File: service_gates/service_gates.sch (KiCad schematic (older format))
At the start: 1 part, among them P1 DIN_41612_128P

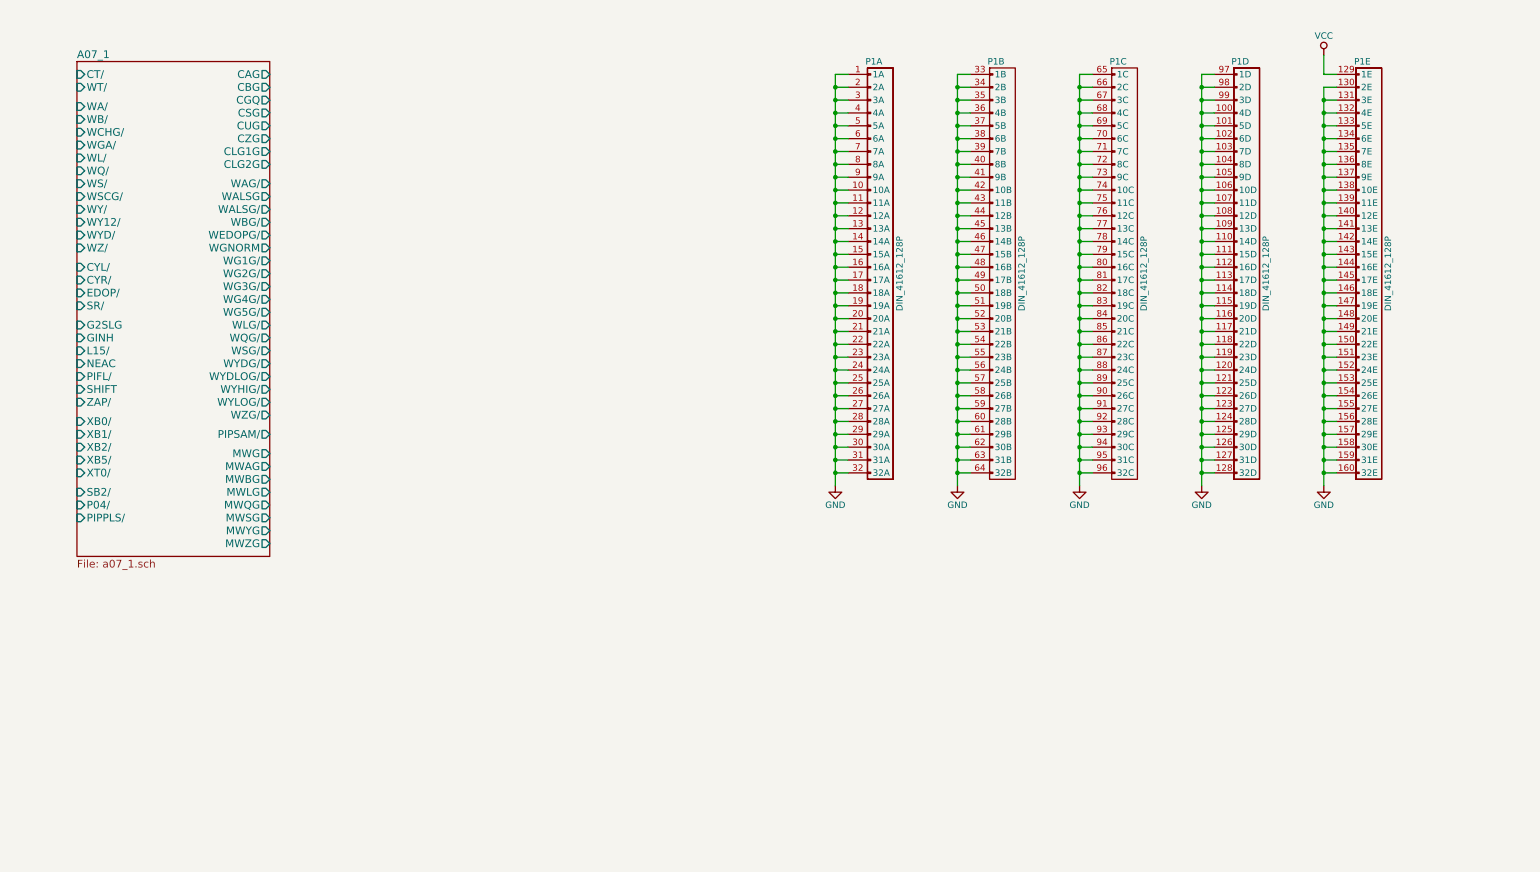
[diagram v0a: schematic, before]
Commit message: Page 2 of the service gates, including some service logic taken from modules 14 and 24 (page 1 got some updates too)
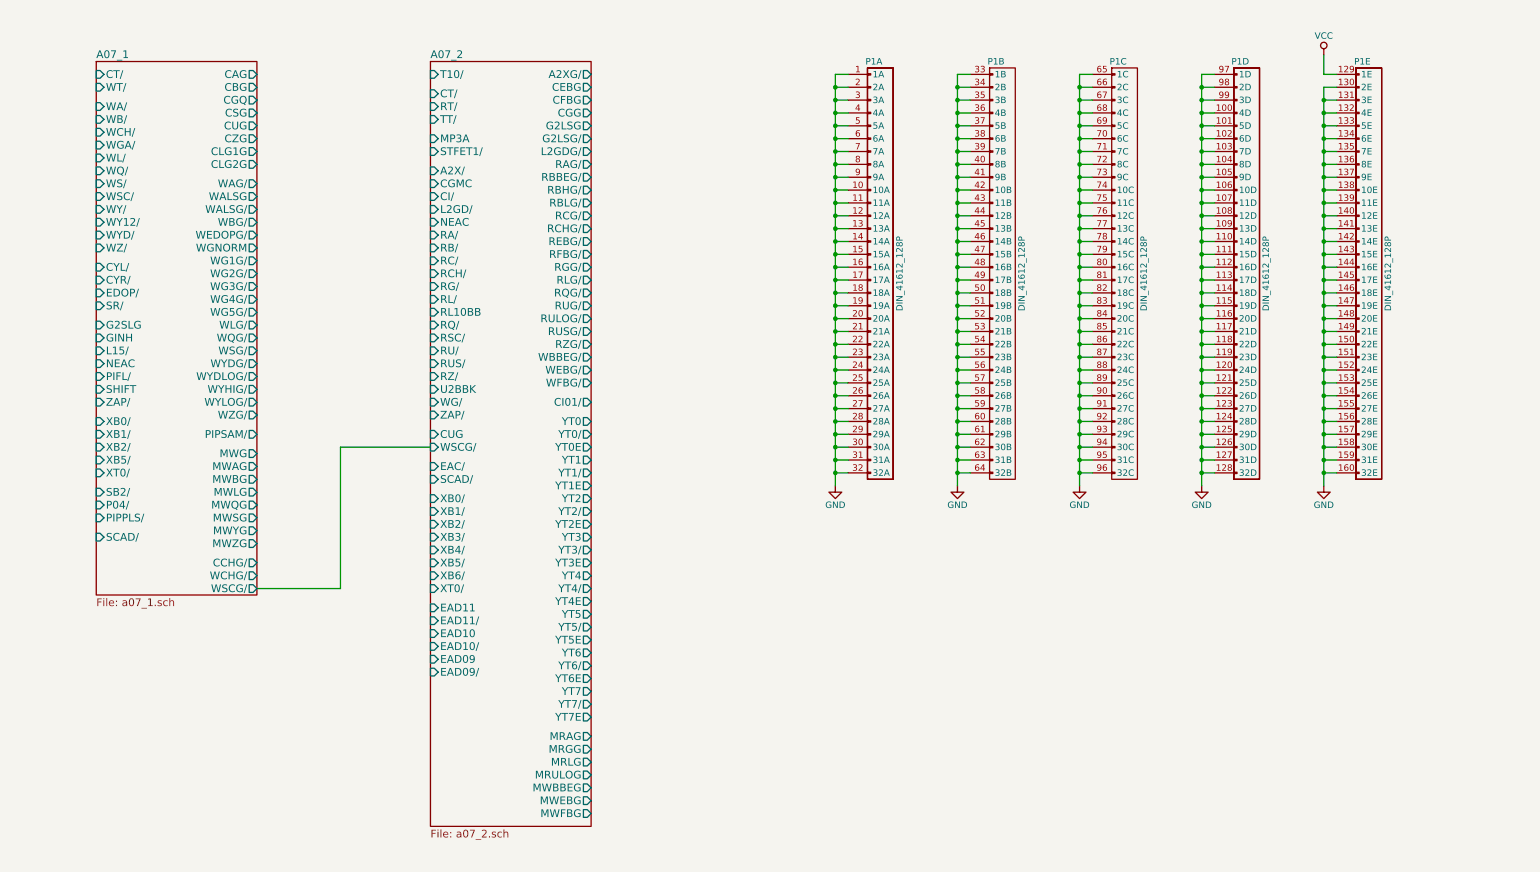
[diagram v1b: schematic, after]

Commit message: Tied in module 7, and corrected lots of errors.
Off the top of my head:
* T12DC/ not actually connected to restart logic in A02-2
* IC12/ and IC13 schematic errors
* Lots of gates moved from later modules up to modules 2-7
* YT0..7 logic dropped from 7, it belongs in 14
* Lots of missing signal breakouts
* ...probably some other things, I should keep a list as I go

All control pulses associated with GOJ1 now behave correctly during
GOJ1.
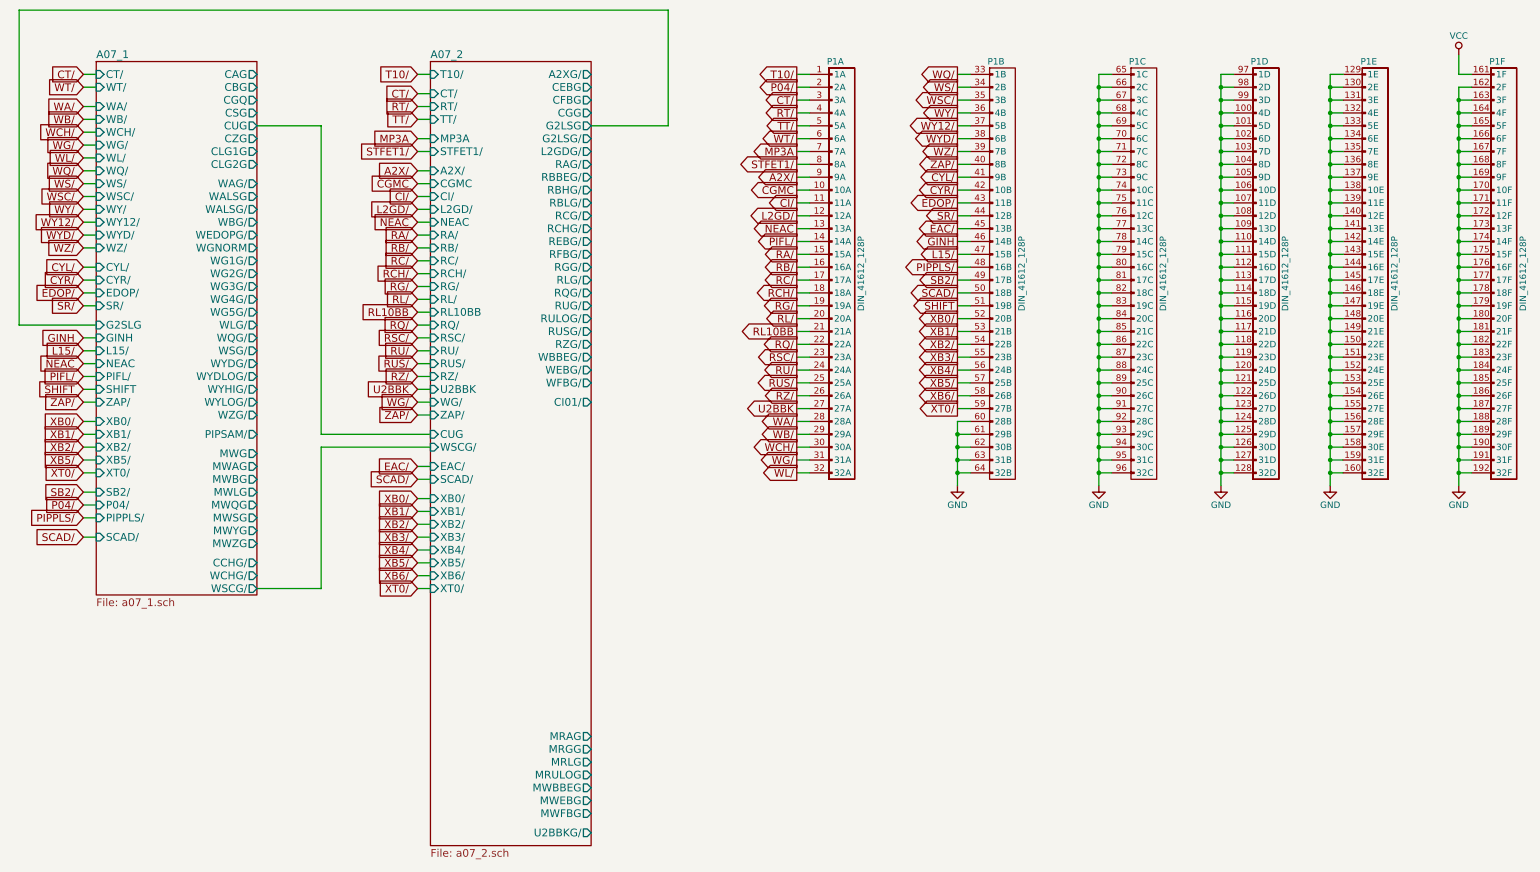
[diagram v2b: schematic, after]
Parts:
- added unit 5 of P1
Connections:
- net GND: now also P1.162 (2F), P1.163 (3F), P1.164 (4F), P1.165 (5F), P1.166 (6F), P1.167 (7F), P1.168 (8F), P1.169 (9F), P1.170 (10F), P1.171 (11F), P1.172 (12F), P1.173 (13F), P1.174 (14F), P1.175 (15F), P1.176 (16F), P1.177 (17F), P1.178 (18F), P1.179 (19F), P1.180 (20F), P1.181 (21F), P1.182 (22F), P1.183 (23F), P1.184 (24F), P1.185 (25F), P1.186 (26F), P1.187 (27F), P1.188 (28F), P1.189 (29F), P1.190 (30F), P1.191 (31F), P1.192 (32F), P1.129 (1E), P1.130 (2E), P1.131 (3E), P1.132 (4E), P1.133 (5E), P1.134 (6E), P1.135 (7E), P1.136 (8E), P1.137 (9E), P1.138 (10E), P1.139 (11E), P1.140 (12E), P1.141 (13E), P1.142 (14E), P1.143 (15E), P1.144 (16E), P1.145 (17E), P1.146 (18E), P1.147 (19E), P1.148 (20E), P1.149 (21E), P1.150 (22E), P1.151 (23E), P1.152 (24E), P1.153 (25E), P1.154 (26E), P1.155 (27E), P1.156 (28E), P1.157 (29E), P1.158 (30E), P1.159 (31E), P1.160 (32E); no longer P1.1 (1A), P1.10 (10A), P1.11 (11A), P1.12 (12A), P1.13 (13A), P1.130 (2E), P1.131 (3E), P1.132 (4E), P1.133 (5E), P1.134 (6E), P1.135 (7E), P1.136 (8E), P1.137 (9E), P1.138 (10E), P1.139 (11E), P1.14 (14A), P1.140 (12E), P1.141 (13E), P1.142 (14E), P1.143 (15E), P1.144 (16E), P1.145 (17E), P1.146 (18E), P1.147 (19E), P1.148 (20E), P1.149 (21E), P1.15 (15A), P1.150 (22E), P1.151 (23E), P1.152 (24E), P1.153 (25E), P1.154 (26E), P1.155 (27E), P1.156 (28E), P1.157 (29E), P1.158 (30E), P1.159 (31E), P1.16 (16A), P1.160 (32E), P1.17 (17A), P1.18 (18A), P1.19 (19A), P1.2 (2A), P1.20 (20A), P1.21 (21A), P1.22 (22A), P1.23 (23A), P1.24 (24A), P1.25 (25A), P1.26 (26A), P1.27 (27A), P1.28 (28A), P1.29 (29A), P1.3 (3A), P1.30 (30A), P1.31 (31A), P1.32 (32A), P1.33 (1B), P1.34 (2B), P1.35 (3B), P1.36 (4B), P1.37 (5B), P1.38 (6B), P1.39 (7B), P1.4 (4A), P1.40 (8B), P1.41 (9B), P1.42 (10B), P1.43 (11B), P1.44 (12B), P1.45 (13B), P1.46 (14B), P1.47 (15B), P1.48 (16B), P1.49 (17B), P1.5 (5A), P1.50 (18B), P1.51 (19B), P1.52 (20B), P1.53 (21B), P1.54 (22B), P1.55 (23B), P1.56 (24B), P1.57 (25B), P1.58 (26B), P1.59 (27B), P1.6 (6A), P1.7 (7A), P1.8 (8A), P1.9 (9A)
- net VCC: now also P1.161 (1F); no longer P1.129 (1E)
- new net A2X/: P1.9 (9A)
- new net CGMC: P1.10 (10A)
- new net CI/: P1.11 (11A)
- new net CT/: P1.3 (3A)
- new net CYL/: P1.41 (9B)
- new net CYR/: P1.42 (10B)
- new net EAC/: P1.45 (13B)
- new net EDOP/: P1.43 (11B)
- new net GINH: P1.46 (14B)
- new net L15/: P1.47 (15B)
- new net L2GD/: P1.12 (12A)
- new net MP3A: P1.7 (7A)
- new net NEAC: P1.13 (13A)
- new net P04/: P1.2 (2A)
- new net PIFL/: P1.14 (14A)
- new net PIPPLS/: P1.48 (16B)
- new net RA/: P1.15 (15A)
- new net RB/: P1.16 (16A)
- new net RC/: P1.17 (17A)
- new net RCH/: P1.18 (18A)
- new net RG/: P1.19 (19A)
- new net RL/: P1.20 (20A)
- new net RL10BB: P1.21 (21A)
- new net RQ/: P1.22 (22A)
- new net RSC/: P1.23 (23A)
- new net RT/: P1.4 (4A)
- new net RU/: P1.24 (24A)
- new net RUS/: P1.25 (25A)
- new net RZ/: P1.26 (26A)
- new net SB2/: P1.49 (17B)
- new net SCAD/: P1.50 (18B)
- new net SHIFT: P1.51 (19B)
- new net SR/: P1.44 (12B)
- new net STFET1/: P1.8 (8A)
- new net T10/: P1.1 (1A)
- new net TT/: P1.5 (5A)
- new net U2BBK: P1.27 (27A)
- new net WA/: P1.28 (28A)
- new net WB/: P1.29 (29A)
- new net WCH/: P1.30 (30A)
- new net WG/: P1.31 (31A)
- new net WL/: P1.32 (32A)
- new net WQ/: P1.33 (1B)
- new net WS/: P1.34 (2B)
- new net WSC/: P1.35 (3B)
- new net WT/: P1.6 (6A)
- new net WY/: P1.36 (4B)
- new net WY12/: P1.37 (5B)
- new net WYD/: P1.38 (6B)
- new net WZ/: P1.39 (7B)
- new net XB0/: P1.52 (20B)
- new net XB1/: P1.53 (21B)
- new net XB2/: P1.54 (22B)
- new net XB3/: P1.55 (23B)
- new net XB4/: P1.56 (24B)
- new net XB5/: P1.57 (25B)
- new net XB6/: P1.58 (26B)
- new net XT0/: P1.59 (27B)
- new net ZAP/: P1.40 (8B)
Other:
- moved on the sheet: P1A, P1C, P1D

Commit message: Tied in module 8, and corrected lots of initial conditions.
The registers and ALU appear to work now, with TC0 and STD2 shuffling things around correctly, and Z counting up as instructions execute.
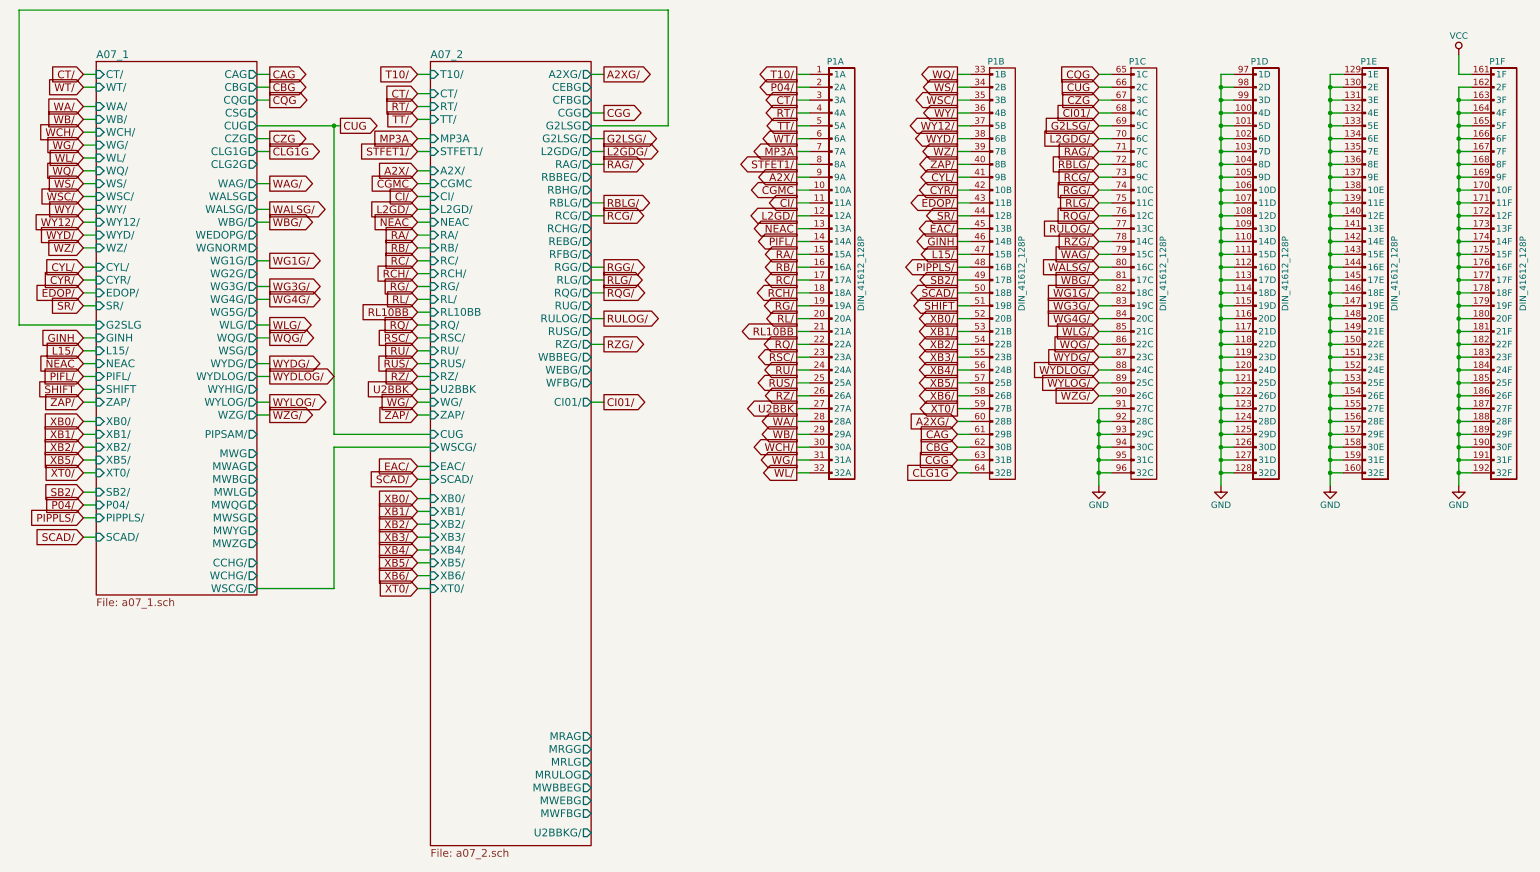
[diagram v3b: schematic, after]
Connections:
- net GND: no longer P1.60 (28B), P1.61 (29B), P1.62 (30B), P1.63 (31B), P1.64 (32B), P1.65 (1C), P1.66 (2C), P1.67 (3C), P1.68 (4C), P1.69 (5C), P1.70 (6C), P1.71 (7C), P1.72 (8C), P1.73 (9C), P1.74 (10C), P1.75 (11C), P1.76 (12C), P1.77 (13C), P1.78 (14C), P1.79 (15C), P1.80 (16C), P1.81 (17C), P1.82 (18C), P1.83 (19C), P1.84 (20C), P1.85 (21C), P1.86 (22C), P1.87 (23C), P1.88 (24C), P1.89 (25C), P1.90 (26C)
- new net A2XG/: P1.60 (28B)
- new net CAG: P1.61 (29B)
- new net CBG: P1.62 (30B)
- new net CGG: P1.63 (31B)
- new net CI01/: P1.68 (4C)
- new net CLG1G: P1.64 (32B)
- new net CQG: P1.65 (1C)
- new net CUG: P1.66 (2C)
- new net CZG: P1.67 (3C)
- new net G2LSG/: P1.69 (5C)
- new net L2GDG/: P1.70 (6C)
- new net RAG/: P1.71 (7C)
- new net RBLG/: P1.72 (8C)
- new net RCG/: P1.73 (9C)
- new net RGG/: P1.74 (10C)
- new net RLG/: P1.75 (11C)
- new net RQG/: P1.76 (12C)
- new net RULOG/: P1.77 (13C)
- new net RZG/: P1.78 (14C)
- new net WAG/: P1.79 (15C)
- new net WALSG/: P1.80 (16C)
- new net WBG/: P1.81 (17C)
- new net WG1G/: P1.82 (18C)
- new net WG3G/: P1.83 (19C)
- new net WG4G/: P1.84 (20C)
- new net WLG/: P1.85 (21C)
- new net WQG/: P1.86 (22C)
- new net WYDG/: P1.87 (23C)
- new net WYDLOG/: P1.88 (24C)
- new net WYLOG/: P1.89 (25C)
- new net WZG/: P1.90 (26C)
